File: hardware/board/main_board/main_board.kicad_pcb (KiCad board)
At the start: 4 copper layers, 80 x 50 mm, 196 parts, among them J2 Conn_01x03_Male, J3 Conn_Triaxial, J4 AudioJack3, J5 USB_C_Receptacle_USB2.0, J6 Barrel_Jack_Switch, J7 Conn_Coaxial, SW2 SW_DIP_x02, U1 74LVCH2T45DC, U10 ADA4891-2, U11 LM27762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

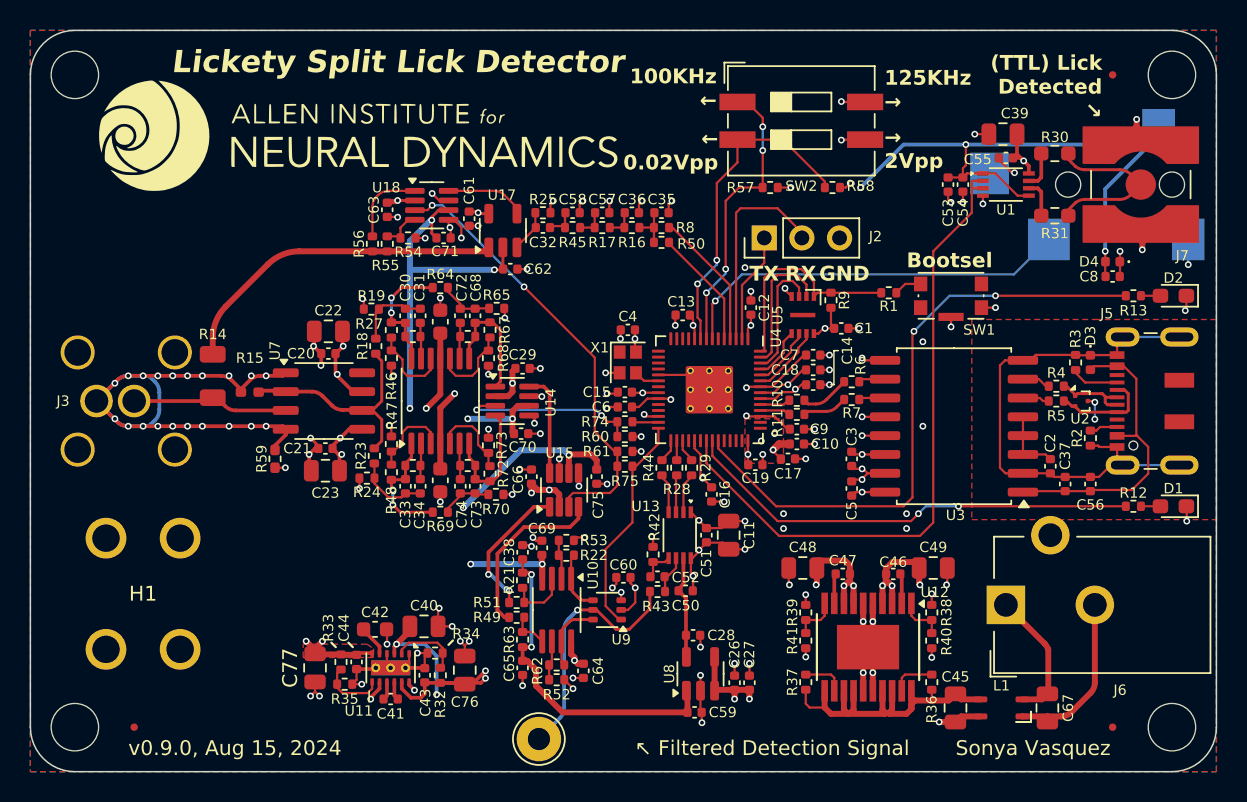
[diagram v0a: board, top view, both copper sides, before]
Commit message: split board into two
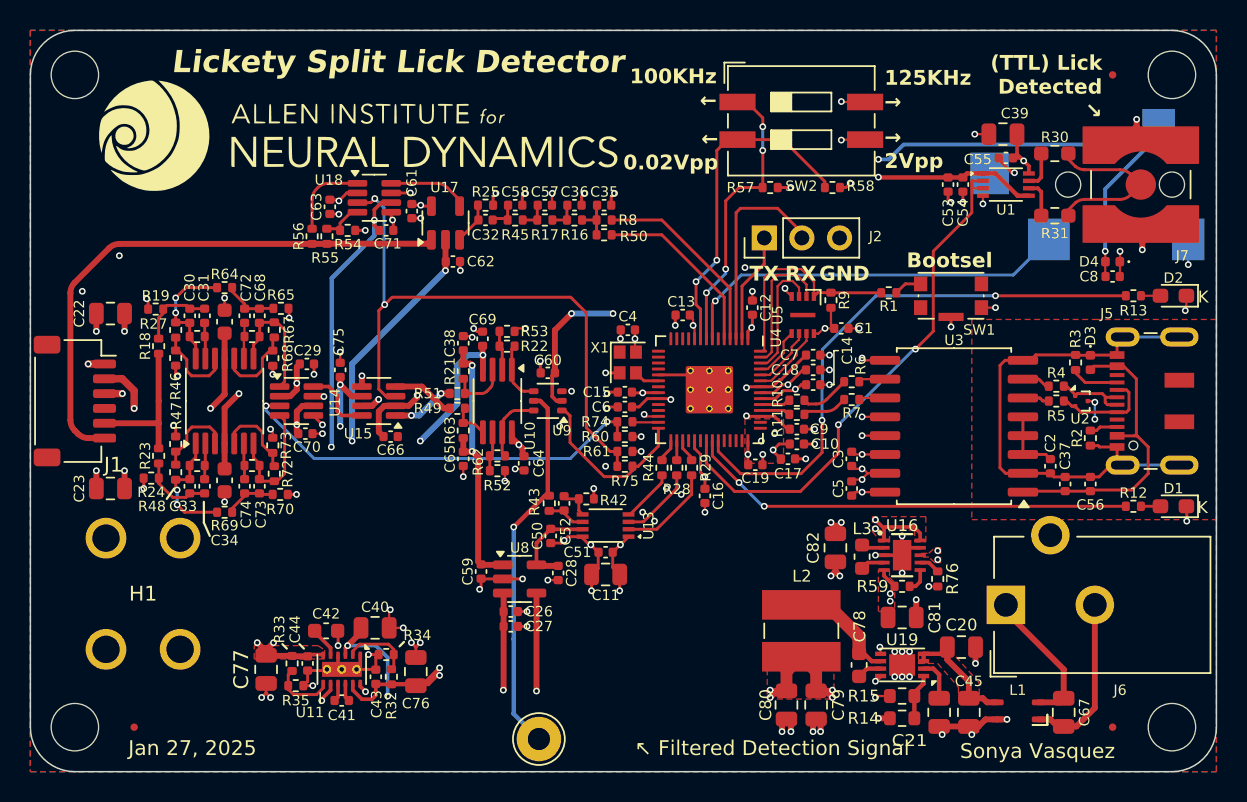
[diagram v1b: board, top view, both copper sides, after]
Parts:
- removed C46, C47: 10nF, Capacitor_SMD:C_0402_1005Metric
- removed C48: 10uF, Capacitor_SMD:C_0805_2012Metric
- removed C49: 22uF, Capacitor_SMD:C_0805_2012Metric
- removed J3: Conn_Triaxial, kicad_component_library:TRB_Trompeter_CBBJR79A_Horizontal
- removed R36, R37: 1M, Resistor_SMD:R_0402_1005Metric
- removed R38: 309K, Resistor_SMD:R_0402_1005Metric
- removed R39: 172K, Resistor_SMD:R_0402_1005Metric
- removed R40, R41: 100K, Resistor_SMD:R_0402_1005Metric
- removed U12: LT3030, Package_SO:ETSSOP-20-1EP_4.4x6.5mm_P0.65mm_EP3x4.2mm
- removed U7: LTC6268xS8-10, Package_SO:SO-8_3.9x4.9mm_P1.27mm
- added C78: 0.1uF, Capacitor_SMD:C_0603_1608Metric, F.Cu at (160.8, 110.8)
- added C79: 10uF, Capacitor_SMD:C_0805_2012Metric, F.Cu at (157.9, 113.5)
- added C80: 10uF, Capacitor_SMD:C_0805_2012Metric, F.Cu at (155.9, 113.5)
- added C81: 10uF, Capacitor_SMD:C_0805_2012Metric, F.Cu at (163.7, 107.6)
- added C82: 22uF, Capacitor_SMD:C_0805_2012Metric, F.Cu at (159.2, 102.9)
- added J1: Conn_01x06_Female, Connector_JST:JST_SH_SM06B-SRSS-TB_1x06-1MP_P1.00mm_Horizontal, F.Cu at (107.9, 93.0)
- added L2: 15uH, kicad_component_library:L_Wuerth_5.5x5.3mm, F.Cu at (156.9, 108.5)
- added L3: 2.2uH, Inductor_SMD:L_0603_1608Metric, F.Cu at (161.0, 103.5)
- added R76: 100K, Resistor_SMD:R_0402_1005Metric, F.Cu at (166.1, 105.0)
- added U16: rt6150b-33gqw, kicad_component_library:WDFN-10-1EP_2.5x2.5mm_P0.5_EP1.25x2.1mm, F.Cu at (163.7, 103.4)
- added U19: MCP16312x-xMNY, Package_DFN_QFN:DFN-8-1EP_3x2mm_P0.5mm_EP1.75x1.45mm, F.Cu at (163.7, 110.8)
- C20: value 100nF -> 10uF; footprint Capacitor_SMD:C_0402_1005Metric -> Capacitor_SMD:C_0805_2012Metric
- C21: value 100nF -> 1uF; footprint Capacitor_SMD:C_0402_1005Metric -> Capacitor_SMD:C_0805_2012Metric
- R14: value 100K -> 52K3; footprint Resistor_SMD:R_1206_3216Metric -> Resistor_SMD:R_0603_1608Metric
- R15: value 100 -> 10K; footprint Resistor_SMD:R_0402_1005Metric_Pad0.72x0.64mm_HandSolder -> Resistor_SMD:R_0603_1608Metric
- R59: value 0 -> 100K; footprint Resistor_SMD:R_0402_1005Metric_Pad0.72x0.64mm_HandSolder -> Resistor_SMD:R_0402_1005Metric
- moved R14 51.9 mm to (163.7, 114.4), turned to 0 degrees
- moved R15 48.5 mm to (163.7, 112.9), turned to 180 degrees
- moved C20 47.1 mm to (167.7, 109.6)
- moved C21 45.1 mm to (166.2, 114.0), turned to -90 degrees
- moved R59 43.2 mm to (163.7, 105.5), turned to 180 degrees
- moved C75 18.7 mm to (125.8, 90.9), turned to 90 degrees
- moved C59 17.3 mm to (135.3, 104.5), turned to 90 degrees
- moved C27 16.5 mm to (137.3, 108.2), turned to 0 degrees
- moved C26 15.8 mm to (137.3, 107.2), turned to 180 degrees
- moved C22 14.7 mm to (110.3, 87.1), turned to 180 degrees
- moved C60 14.7 mm to (139.8, 91.1)
- moved C38 14.7 mm to (134.1, 89.1)
- moved C69 14.7 mm to (135.4, 88.8)
- moved R21 14.7 mm to (134.1, 91.0)
- moved R22 14.7 mm to (137.1, 89.3)
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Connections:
- net +3.3V renamed +3V3
- C20 pad 1: GND -> Net-(U19-EN)
- C20 pad 2: +2V5 -> GND
- C21 pad 1: -2V5 -> Net-(U19-V_{CC})
- C45 pad 1: IN1 -> Net-(U19-EN)
- L1 pad 3: IN1 -> Net-(U19-EN)
- R14 pad 1: /100KHz Sine Wave/VSINE -> +5V
- R14 pad 2: /Lick Detection Analog Front End/triax_core -> Net-(U19-Vfb)
- R15 pad 1: /Lick Detection Analog Front End/triax_inner_shield -> Net-(U19-Vfb)
- R15 pad 2: Net-(U7--) -> GND
- R18 pad 1: Net-(U7--) -> /Lick Detection Analog Front End/VBUF
- R23 pad 2: Net-(U7--) -> /Lick Detection Analog Front End/VBUF
- R59 pad 1: GND -> Net-(U16-EN)
- R59 pad 2: /Lick Detection Analog Front End/triax_inner_shield -> +5V
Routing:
- net /Lick Detection Analog Front End/triax_inner_shield: track 42.0 -> 0.00 mm, vias 20 -> 0
- net IN1: track 23.8 -> 0.00 mm
- net Net-(U7--): track 16.1 -> 0.00 mm
- net FREQ_SEL_2V5: track 12.2 -> 28.3 mm
- net /100KHz Sine Wave/VSINE: track 22.7 -> 37.3 mm
- net GAIN_SEL_2V5: track 30.2 -> 41.7 mm
- net /Lick Detection Analog Front End/triax_core: track 10.4 -> 0.00 mm
- net +5V: track 29.1 -> 39.4 mm, vias 11 -> 16
- net /Lick Detection Analog Front End/VBUF: track 0.00 -> 10.0 mm
- net /Harp Core RP2040 + Isolated USB/TTL_OUT: track 44.8 -> 35.9 mm, vias 0 -> 2
- net Net-(R43-Pad2): track 16.9 -> 25.4 mm
- net Net-(U19-EN): track 0.00 -> 8.35 mm
- net Net-(R49-Pad1): track 12.0 -> 4.26 mm
- net Net-(U19-SW): track 0.00 -> 7.58 mm
- net +3V3: track 93.1 -> 98.4 mm, vias 29 -> 30
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- added copper zone on F.Cu, net +5V
- added copper zone on F.Cu, net Net-(U19-EN)
- removed copper zone on In1.Cu, net /Lick Detection Analog Front End/triax_inner_shield
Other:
- board text added: "0356-E-001-001.000.000"
- board text added: "6-30VDC"
- board text added: "Cable Buffer Board Input"
- board text added: "Jan 27, 2025"
- board text added: "K"
- board text removed: "6-20VDC"
- board text removed: "v0.9.0, Aug 15, 2024"
- board text removed: "↑ Lick Tube Input (Triax)"

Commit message: update buffer board soldermask cutout
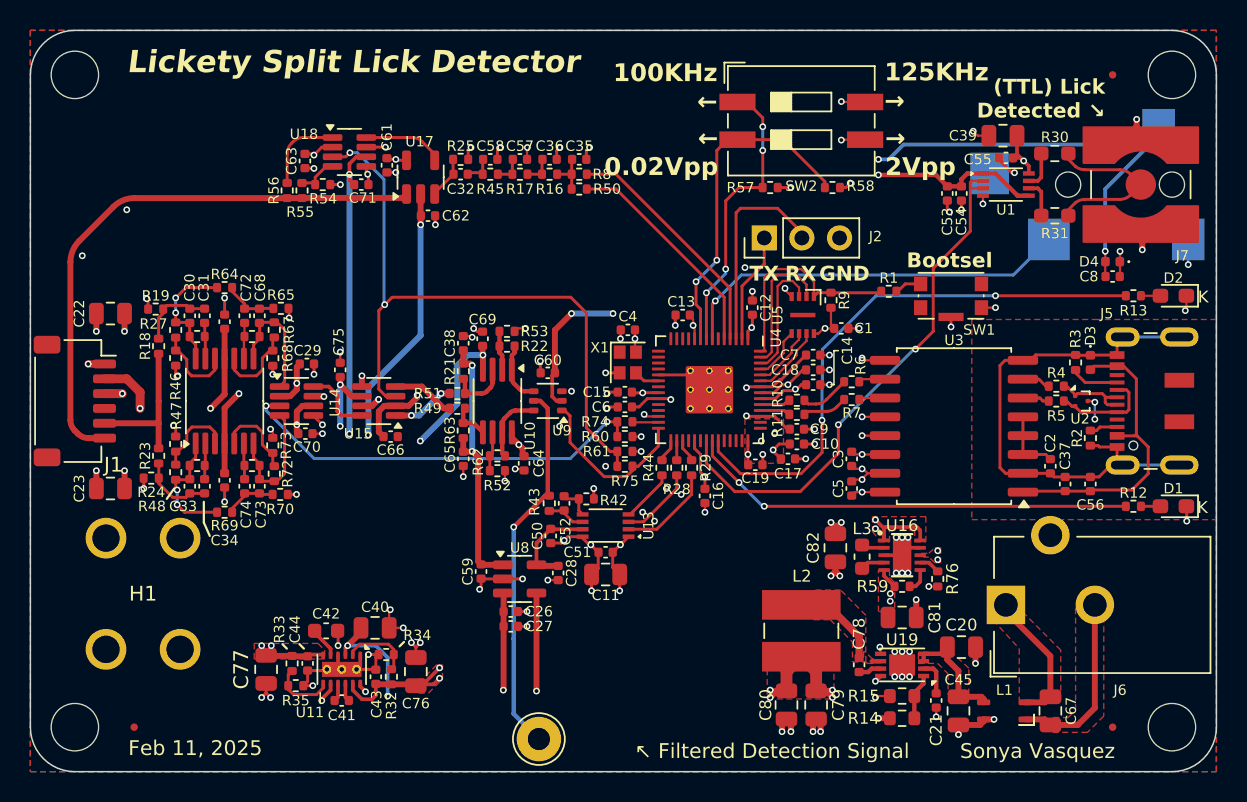
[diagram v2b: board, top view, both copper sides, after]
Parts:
- removed G2: LOGO, LOGO
- C21: footprint Capacitor_SMD:C_0805_2012Metric -> Capacitor_SMD:C_0402_1005Metric
- C24, C25: footprint Capacitor_SMD:C_0603_1608Metric -> Capacitor_SMD:C_0402_1005Metric
- C4: value 10nF -> 100nF
- C45, C67: value 3.3uF -> 10uF
- C78: value 0.1uF -> 100nF; footprint Capacitor_SMD:C_0603_1608Metric -> Capacitor_SMD:C_0402_1005Metric
- R1: value 1K -> 1K05
- moved C32 3.52 mm to (133.9, 77.7)
- moved C35 3.52 mm to (141.9, 76.7)
- moved C36 3.52 mm to (139.9, 76.7)
- moved C57 3.52 mm to (137.9, 76.7)
- moved C58 3.52 mm to (135.9, 76.7)
- moved C61 3.52 mm to (128.9, 77.1)
- moved C62 3.52 mm to (131.7, 80.5)
- moved R16 3.52 mm to (139.9, 77.7)
- moved R17 3.52 mm to (137.9, 77.7)
- moved R25 3.52 mm to (133.9, 76.7)
- moved R45 3.52 mm to (135.9, 77.7)
- moved R50 3.52 mm to (141.9, 78.7)
- moved R55 3.52 mm to (123.2, 78.8)
- moved R56 3.52 mm to (122.2, 78.8)
- moved R8 3.52 mm to (141.9, 77.7)
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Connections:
- C78 pad 1: Net-(U19-BOOST) -> Net-(U19-SW)
- C78 pad 2: Net-(U19-SW) -> Net-(U19-BOOST)
- R1 pad 1: /Harp Core RP2040 + Isolated USB/USB_Boot -> /Harp Core RP2040 + Isolated USB/QSPI_CS
- R1 pad 2: /Harp Core RP2040 + Isolated USB/QSPI_CS -> /Harp Core RP2040 + Isolated USB/USB_Boot
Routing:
- net GAIN_SEL_2V5: track 41.7 -> 45.7 mm
- net /100KHz Sine Wave/100KHZ_IN: track 13.4 -> 16.3 mm
- net /100KHz Sine Wave/125KHZ_IN: track 12.2 -> 15.2 mm
- net GND: track 129.7 -> 132.5 mm, vias 126 -> 129
- net /100KHz Sine Wave/VSINE: track 37.3 -> 38.3 mm
- net +3V3: track 98.4 -> 99.4 mm
- net GND2: track 11.5 -> 12.3 mm
- net Net-(U19-SW): track 7.58 -> 6.81 mm
- net -2V5: track 69.6 -> 70.3 mm
- added copper zone on F.Cu, net +12V
- added copper zone on F.Cu, net +2V5
- added copper zone on F.Cu, net GND2
- added copper zone on F.Cu, net Net-(U19-SW)
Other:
- board text added: "Feb 11, 2025"
- board text removed: "Jan 27, 2025"
